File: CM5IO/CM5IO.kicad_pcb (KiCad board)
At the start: 4 copper layers, 59.7 x 78 mm, 62 parts, among them J1 POWER TERMINAL, J11 USB_C_Receptacle_USB2.0, J12 USB3_A, J16 Conn_01x22_Female, J2 Conn_02x06_Odd_Even, J22 46765-1301, J4 J_PSU_EN, J5 Conn_01x22_Female, J7 Micro_SD_Card_Det, J8 THD-20-R, SW1 Right angle Tact button, U12 RT9742SNGV, U18 RT9742GGJ5, U6 AP22653W6

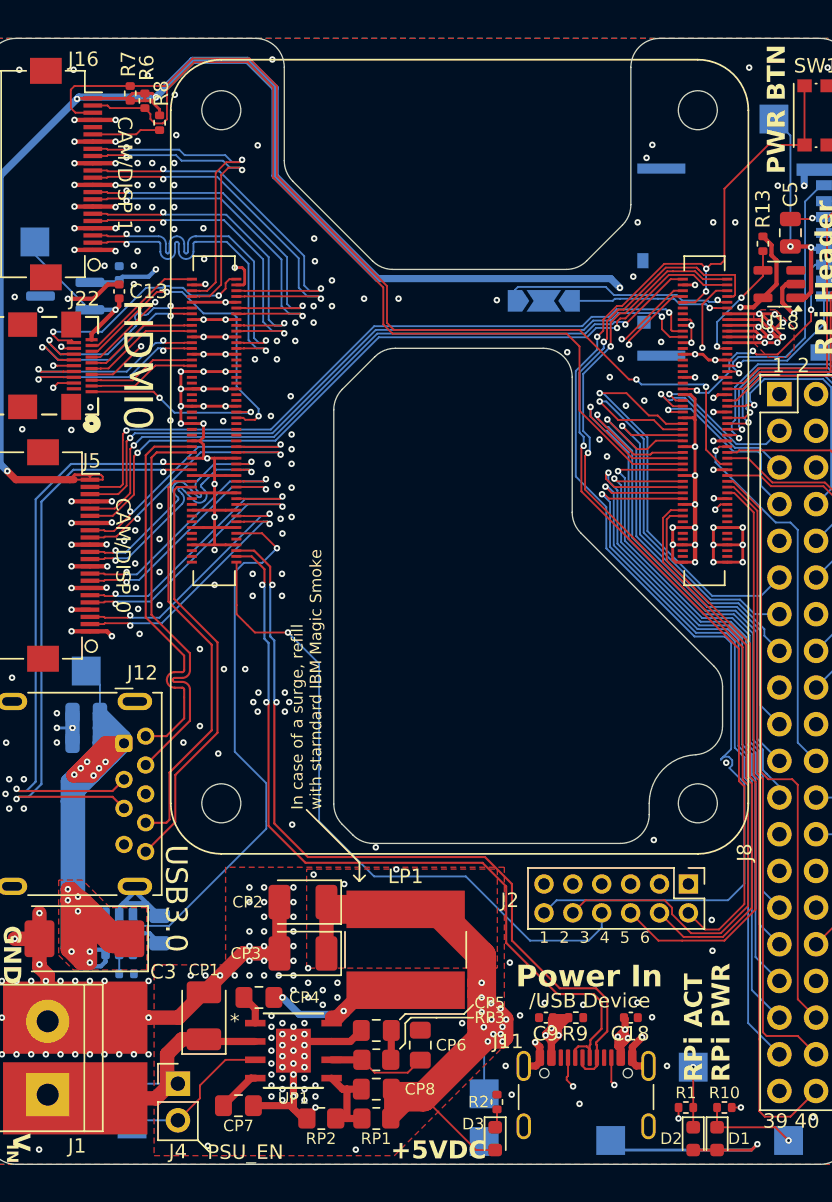
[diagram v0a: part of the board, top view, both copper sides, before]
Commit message: small fixes for ground planes, logo added, minor other changes
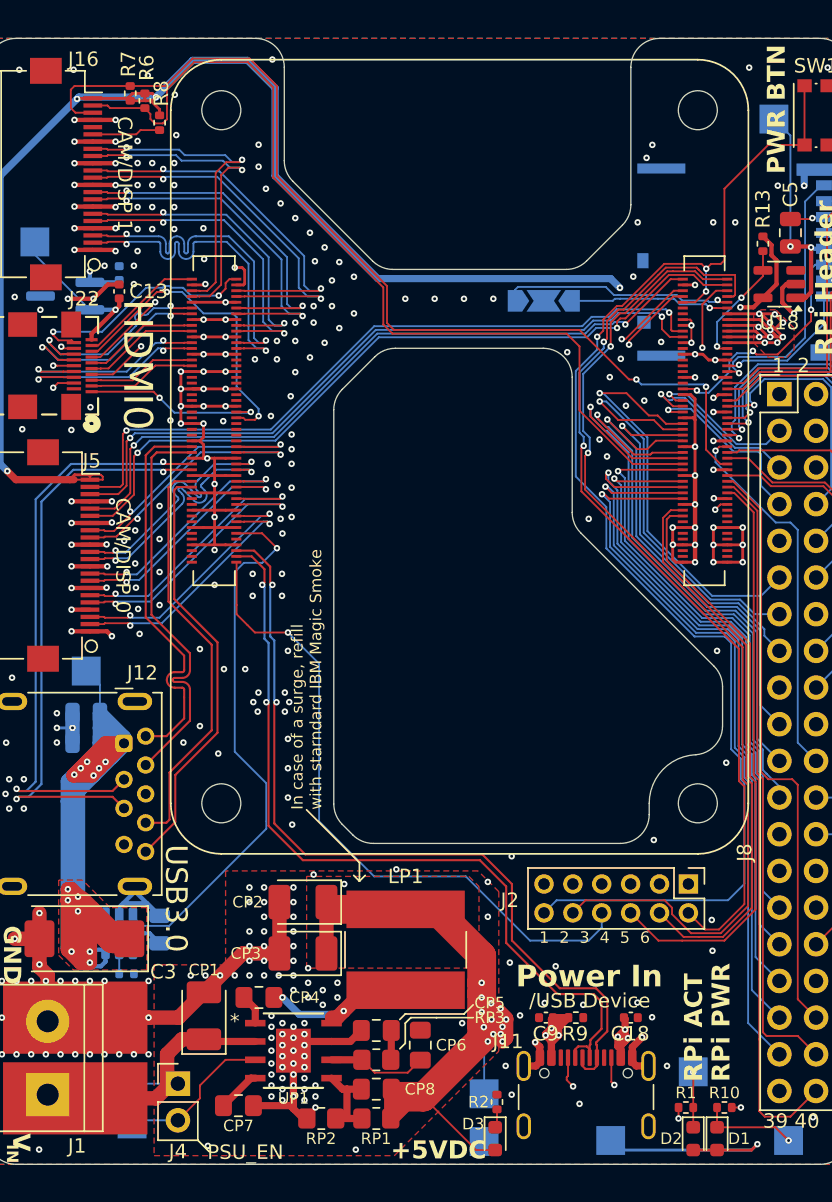
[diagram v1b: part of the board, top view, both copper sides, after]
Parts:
- moved TP7 0.32 mm to (195.2, 140.1)
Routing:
- net /+5v: track 258.6 -> 292.4 mm
- net /CM5_GPIO ( Ethernet, GPIO, SDCARD)/PWR_BUT: track 91.7 -> 90.4 mm
- net GND: track 781.0 -> 781.3 mm, vias 316 -> 339
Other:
- board text added: "CM5IO drone board"
- board text added: "rev 1.0, 01.2026 AGH Drone Engineering"

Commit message: whatever
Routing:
- net /+5v: track 292.4 -> 303.5 mm, vias 31 -> 32
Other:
- board text added: "Built-in AP64501 converter supplies 5V, 5A MAX. 3V3 line is supplied by RPi, 600mA MAX. Vin MAX = 40V but is limited by CP1 DO NOT CONNECT USB AND Vin AT ONCE!"
- board text removed: "Built-in AP64501 converter supplies 5V, 5A MAX. 3V3 line is supplied by RPi, 600mA MAX. Vin MAX = 40V but is limited by CP1"
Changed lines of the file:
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@@
 		(pcbplotparams
 			(layerselection 0x00000000_00000000_5555555f_ffffffff)
-			(plot_on_all_layers_selection 0x00000000_00000000_00000000_0a000022)
+			(plot_on_all_layers_selection 0x00000000_00000000_00000000_0a000000)
 			(disableapertmacros no)
 			(usegerberextensions no)
@@
 		(tags "Through hole pin header THT 1x02 2.54mm single row")
 		(property "Reference" "J4"
-			(at 0 4.699 0)
+			(at -0.889 -2.286 0)
 			(layer "F.SilkS")
 			(effects
 				(font
-					(size 1 1)
-					(thickness 0.15)
+					(size 0.8 0.8)
+					(thickness 0.1)
 				)
 			)
@@
 		(tags "terminal block bornier2")
 		(property "Reference" "J1"
-			(at -3.556 2.032 180)
+			(at -3.175 -0.254 180)
 			(layer "F.SilkS")
 			(effects
 				(font
-					(size 1 1)
-					(thickness 0.15)
+					(size 0.8 0.8)
+					(thickness 0.1)
 				)
 			)
@@
 		)
 	)
-	(gr_text "Built-in AP64501 \nconverter supplies \n5V, 5A MAX.\n\n3V3 line is \nsupplied by RPi, \n600mA MAX.\n\nVin MAX = 40V\nbut is limited by CP1"
-		(at 169.998401 110.425601 0)
+	(gr_text "Built-in AP64501 \nconverter supplies \n5V, 5A MAX.\n\n3V3 line is \nsupplied by RPi, \n600mA MAX.\n\nVin MAX = 40V\nbut is limited by CP1\n\nDO NOT CONNECT \nUSB AND Vin \nAT ONCE!"
+		(at 169.998401 112.593 0)
 		(layer "B.SilkS")
 		(effects
@@
 	)
 	(via
-		(at 168.892 126.436)
+		(at 169.019 126.182)
 		(size 0.45)
 		(drill 0.2)
@@
 	)
 	(segment
+		(start 169.781 130.119)
+		(end 169.781 128.341)
+		(width 1)
+		(layer "F.Cu")
+		(net 17)
+	)
+	(segment
 		(start 200.795 87.6)
 		(end 199.753 87.6)
@@
 	(segment
 		(start 169.781 131.897)
-		(end 169.781 128.341)
+		(end 169.781 130.119)
 		(width 1)
 		(layer "F.Cu")
@@
 	)
 	(via
+		(at 169.781 130.119)
+		(size 0.45)
+		(drill 0.2)
+		(layers "F.Cu" "B.Cu")
+		(net 17)
+	)
+	(via
 		(at 201.404 88.209)
 		(size 0.45)
@@
 	)
 	(segment
-		(start 155.27 85.42)
-		(end 155.43 85.26)
+		(start 158.224 131.196)
+		(end 158.532 130.888)
 		(width 0.3)
 		(layer "B.Cu")
@@
 	)
 	(segment
-		(start 184.961 137.568)
-		(end 185.861 137.568)
-		(width 0.5)
+		(start 155.27 85.42)
+		(end 155.43 85.26)
+		(width 0.3)
 		(layer "B.Cu")
 		(net 17)
@@
 	)
 	(segment
+		(start 158.532 130.888)
+		(end 169.012 130.888)
+		(width 0.3)
+		(layer "B.Cu")
+		(net 17)
+	)
+	(segment
 		(start 153.398 85.42)
 		(end 153.398 84.653)
@@
 		(layer "B.Cu")
 		(net 17)
+	)
+	(segment
+		(start 169.012 130.888)
+		(end 169.781 130.119)
+		(width 0.3)
+		(layer "B.Cu")
+		(net 17)
